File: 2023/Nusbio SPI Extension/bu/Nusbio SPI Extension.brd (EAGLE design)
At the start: 44 x 50 mm, 6 parts

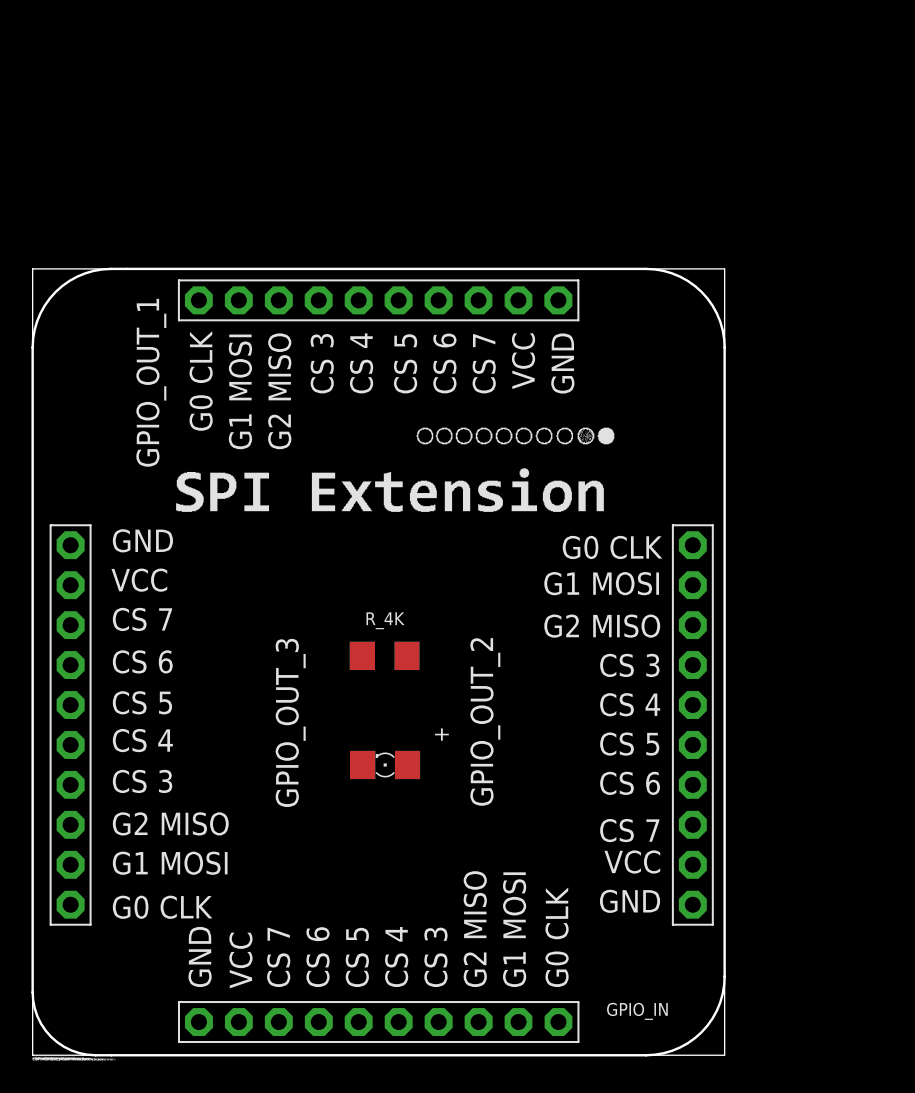
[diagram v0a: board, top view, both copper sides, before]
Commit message: Nusbio I2C Extension
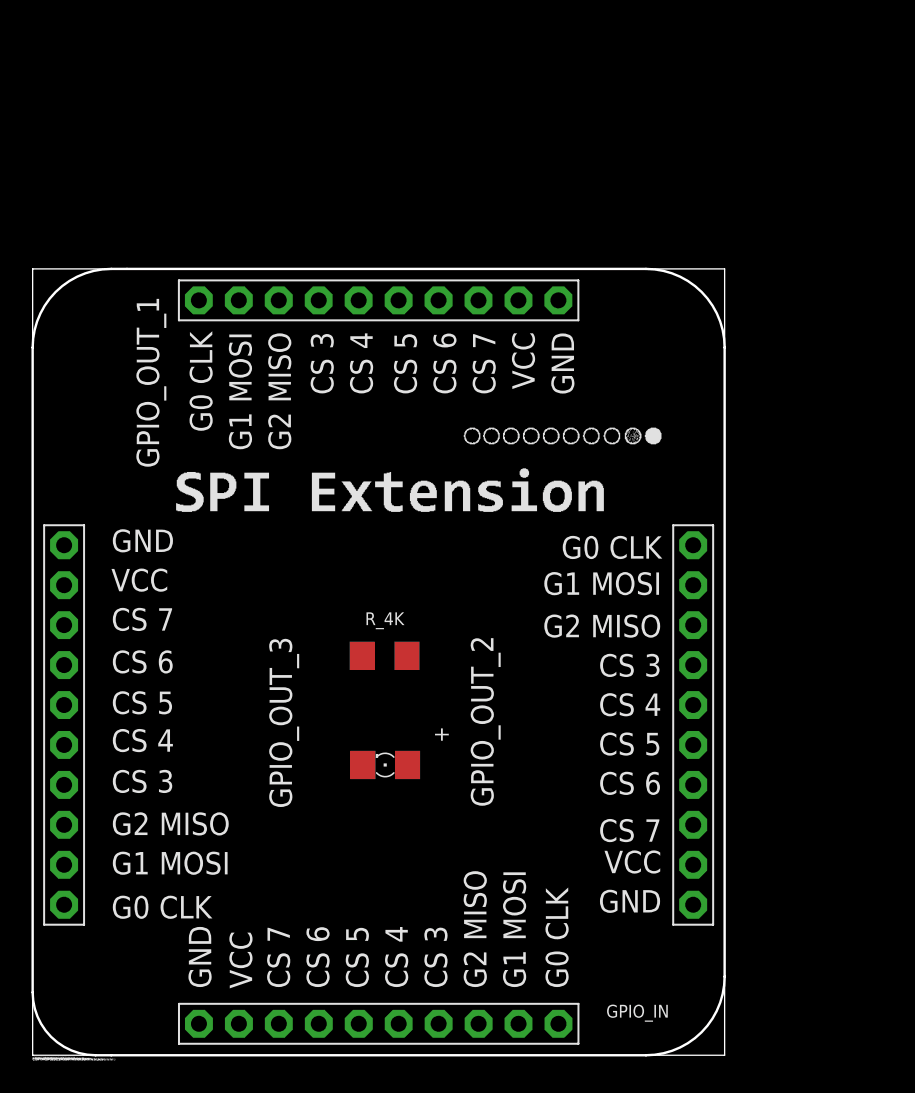
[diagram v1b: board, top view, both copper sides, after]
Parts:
- moved GPIO_OUT_3 0.41 mm to (2.00, 21.0)
- moved GPIO_IN 0.11 mm to (22.0, 2.00)

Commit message: Nusbio v2 pcb and SPIExtension v 1 2023/05
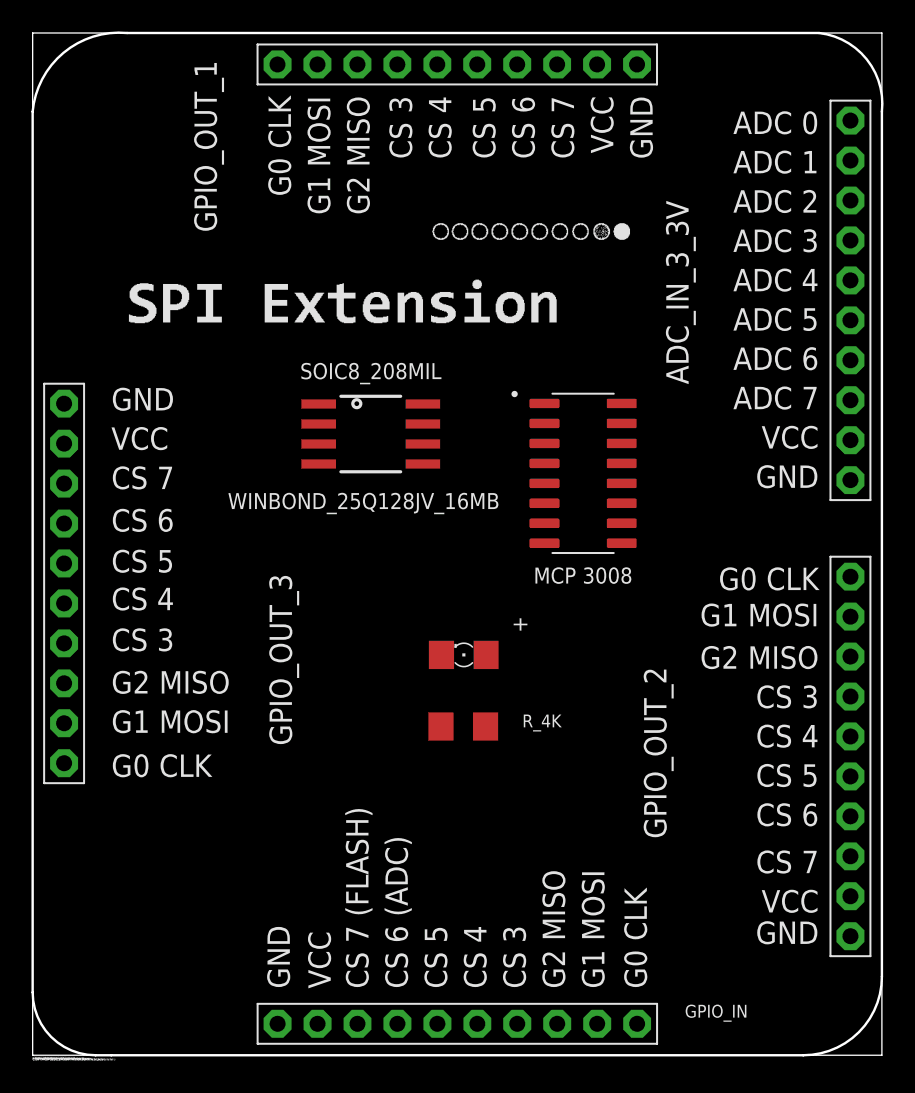
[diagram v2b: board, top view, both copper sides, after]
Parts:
- added ADC_IN_3_3V: PINHD-1X10, adafruit:1X10-BIG
- added MCP_3008_3_3V: MCP3008-I/SL, MCP3008-I_SL:SOIC127P600X175-16N
- added SOIC8_208MIL: (no value), microbuilder:SOIC8_208MIL
- moved GPIO_OUT_1 15.8 mm to (27.0, 63.0)
- moved GPIO_OUT_2 10.2 mm to (52.0, 19.0)
- moved GPIO_OUT_3 9.00 mm to (2.00, 30.0)
- moved LED_POWER 8.60 mm to (27.4, 25.5)
- moved R_4K 6.73 mm to (27.4, 20.9)
- moved GPIO_IN 5.00 mm to (27.0, 2.00)
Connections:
- new net ADC0: ADC_IN_3_3V.1, MCP_3008_3_3V.1
- new net ADC1: ADC_IN_3_3V.2, MCP_3008_3_3V.2
- new net ADC2: ADC_IN_3_3V.3, MCP_3008_3_3V.3
- new net ADC3: ADC_IN_3_3V.4, MCP_3008_3_3V.4
- new net ADC4: ADC_IN_3_3V.5, MCP_3008_3_3V.5
- new net ADC5: ADC_IN_3_3V.6, MCP_3008_3_3V.6
- new net ADC6: ADC_IN_3_3V.7, MCP_3008_3_3V.7
- new net ADC7: ADC_IN_3_3V.8, MCP_3008_3_3V.8
- net GND: now also ADC_IN_3_3V.10, MCP_3008_3_3V.14, MCP_3008_3_3V.9, SOIC8_208MIL.4
- net GPIO0: now also MCP_3008_3_3V.13, SOIC8_208MIL.6
- net GPIO1: now also MCP_3008_3_3V.11, SOIC8_208MIL.5
- net GPIO2: now also MCP_3008_3_3V.12, SOIC8_208MIL.2
- net GPIO6: now also MCP_3008_3_3V.10
- net GPIO7: now also SOIC8_208MIL.1
- net VCC: now also ADC_IN_3_3V.9, MCP_3008_3_3V.15, MCP_3008_3_3V.16, SOIC8_208MIL.3, SOIC8_208MIL.7, SOIC8_208MIL.8
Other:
- board size 44 x 50 mm -> 54 x 65 mm
- board text added: "ADC 0"
- board text added: "ADC 1"
- board text added: "ADC 2"
- board text added: "ADC 3"
- board text added: "ADC 4"
- board text added: "ADC 5"
- board text added: "ADC 6"
- board text added: "ADC 7"
- board text added: "CS 6 (ADC)"
- board text added: "CS 7 (FLASH)"
- board text added: "MCP 3008"
- board text added: "WINBOND_25Q128JV_16MB"

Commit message: Nusbio v2 pcb and SPIExtension v 1 2023/05
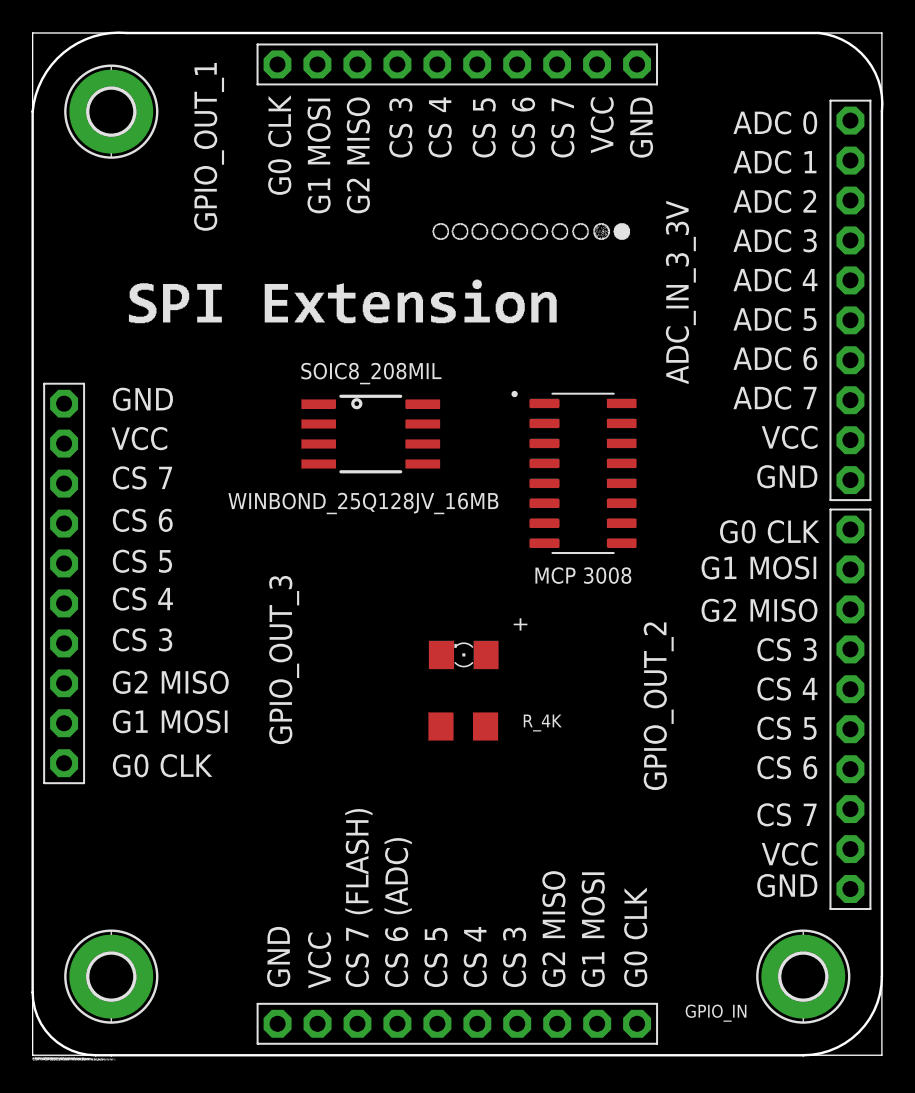
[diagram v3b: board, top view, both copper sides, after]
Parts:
- added H1, H2, H3: MOUNT-PAD-ROUND2.8, holes:2,8-PAD
- moved GPIO_OUT_2 3.00 mm to (52.0, 22.0)
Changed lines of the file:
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@@
 <text x="5" y="38.5" size="1.4224" layer="25" rot="R180" align="top-right">VCC</text>
 <text x="5" y="41" size="1.4224" layer="25" rot="R180" align="top-right">GND</text>
-<text x="50" y="28.7" size="1.4224" layer="25" rot="R180">G1 MOSI</text>
-<text x="50" y="26" size="1.4224" layer="25" rot="R180">G2 MISO</text>
-<text x="50" y="23.5" size="1.4224" layer="25" rot="R180">CS 3</text>
-<text x="50" y="21" size="1.4224" layer="25" rot="R180">CS 4</text>
-<text x="50" y="18.5" size="1.4224" layer="25" rot="R180">CS 5</text>
-<text x="50" y="16" size="1.4224" layer="25" rot="R180">CS 6</text>
-<text x="50" y="31" size="1.4224" layer="25" rot="R180">G0 CLK</text>
-<text x="50" y="13" size="1.4224" layer="25" rot="R180">CS 7</text>
-<text x="50" y="10.5" size="1.4224" layer="25" rot="R180">VCC</text>
-<text x="50" y="8.5" size="1.4224" layer="25" rot="R180">GND</text>
+<text x="50" y="31.7" size="1.4224" layer="25" rot="R180">G1 MOSI</text>
+<text x="50" y="29" size="1.4224" layer="25" rot="R180">G2 MISO</text>
+<text x="50" y="26.5" size="1.4224" layer="25" rot="R180">CS 3</text>
+<text x="50" y="24" size="1.4224" layer="25" rot="R180">CS 4</text>
+<text x="50" y="21.5" size="1.4224" layer="25" rot="R180">CS 5</text>
+<text x="50" y="19" size="1.4224" layer="25" rot="R180">CS 6</text>
+<text x="50" y="34" size="1.4224" layer="25" rot="R180">G0 CLK</text>
+<text x="50" y="16" size="1.4224" layer="25" rot="R180">CS 7</text>
+<text x="50" y="13.5" size="1.4224" layer="25" rot="R180">VCC</text>
+<text x="50" y="11.5" size="1.4224" layer="25" rot="R180">GND</text>
 <rectangle x1="6.488984375" y1="46.5478625" x2="7.136684375" y2="46.5940875" layer="25"/>
 <rectangle x1="19.7909625" y1="46.5478625" x2="20.3904" y2="46.5940875" layer="25"/>
@@
 <attribute name="VALUE" x="28.6878" y="27.9967" size="1.27" layer="27" rot="R180"/>
 </element>
-<element name="GPIO_OUT_2" library="adafruit" package="1X10-BIG" value="PINHD-1X10" x="52" y="19" smashed="yes" rot="R270">
-<attribute name="NAME" x="39.5898" y="19.231" size="1.4224" layer="25" ratio="10" rot="R270" align="center"/>
+<element name="GPIO_OUT_2" library="adafruit" package="1X10-BIG" value="PINHD-1X10" x="52" y="22" smashed="yes" rot="R270">
+<attribute name="NAME" x="39.5898" y="22.231" size="1.4224" layer="25" ratio="10" rot="R270" align="center"/>
 </element>
 <element name="GPIO_OUT_3" library="adafruit" package="1X10-BIG" value="PINHD-1X10" x="2" y="30" smashed="yes" rot="R90">
@@
 <attribute name="NAME" x="41" y="48.5" size="1.4224" layer="25" ratio="10" rot="R270" align="center"/>
 </element>
+<element name="H2" library="holes" library_urn="urn:adsk.eagle:library:237" package="2,8-PAD" package3d_urn="urn:adsk.eagle:package:14281/1" value="MOUNT-PAD-ROUND2.8" x="5" y="60" smashed="yes">
+<attribute name="POPULARITY" value="6" x="5" y="60" size="1.778" layer="27" display="off"/>
+</element>
+<element name="H1" library="holes" library_urn="urn:adsk.eagle:library:237" package="2,8-PAD" package3d_urn="urn:adsk.eagle:package:14281/1" value="MOUNT-PAD-ROUND2.8" x="5" y="5" smashed="yes">
+<attribute name="POPULARITY" value="6" x="5" y="5" size="1.778" layer="27" display="off"/>
+</element>
+<element name="H3" library="holes" library_urn="urn:adsk.eagle:library:237" package="2,8-PAD" package3d_urn="urn:adsk.eagle:package:14281/1" value="MOUNT-PAD-ROUND2.8" x="49" y="5" smashed="yes">
+<attribute name="POPULARITY" value="6" x="49" y="5" size="1.778" layer="27" display="off"/>
+</element>
 </elements>
 <signals>
@@
 <wire x1="18.185" y1="37.595" x2="37.455" y2="38.905" width="0" layer="19" extent="1-1"/>
 <wire x1="2" y1="41.43" x2="18.185" y2="37.595" width="0" layer="19" extent="1-1"/>
-<wire x1="52" y1="7.57" x2="28.7984" y2="20.8998" width="0" layer="19" extent="1-1"/>
+<wire x1="52" y1="10.57" x2="28.7984" y2="20.8998" width="0" layer="19" extent="1-1"/>
 </signal>
 <signal name="VCC">
@@
 <wire x1="28.8398" y1="25.4567" x2="24.815" y2="40.135" width="0" layer="19" extent="1-1"/>
 <wire x1="18.114771875" y1="2" x2="28.8398" y2="25.4567" width="0" layer="19" extent="1-1"/>
-<wire x1="52" y1="10.11" x2="28.8398" y2="25.4567" width="0" layer="19" extent="1-1"/>
+<wire x1="52" y1="13.11" x2="28.8398" y2="25.4567" width="0" layer="19" extent="1-1"/>
 </signal>
 <signal name="GPIO6">
@@
 <contactref element="MCP_3008_3_3V" pad="10"/>
 <wire x1="37.455" y1="33.825" x2="30.81" y2="63" width="0" layer="19" extent="1-1"/>
-<wire x1="52" y1="15.19" x2="37.455" y2="33.825" width="0" layer="19" extent="1-1"/>
-<wire x1="23.194771875" y1="2" x2="52" y2="15.19" width="0" layer="19" extent="1-1"/>
+<wire x1="52" y1="18.19" x2="37.455" y2="33.825" width="0" layer="19" extent="1-1"/>
+<wire x1="23.194771875" y1="2" x2="52" y2="18.19" width="0" layer="19" extent="1-1"/>
 <wire x1="2" y1="33.81" x2="23.194771875" y2="2" width="0" layer="19" extent="1-1"/>
 </signal>
@@
 <wire x1="2" y1="36.35" x2="18.185" y2="41.405" width="0" layer="19" extent="1-1"/>
 <wire x1="20.654771875" y1="2" x2="2" y2="36.35" width="0" layer="19" extent="1-1"/>
-<wire x1="52" y1="12.65" x2="20.654771875" y2="2" width="0" layer="19" extent="1-1"/>
+<wire x1="52" y1="15.65" x2="20.654771875" y2="2" width="0" layer="19" extent="1-1"/>
 </signal>
 <signal name="GPIO4">
@@
 <contactref element="GPIO_OUT_2" pad="5"/>
 <contactref element="GPIO_OUT_3" pad="5"/>
-<wire x1="52" y1="20.27" x2="25.73" y2="63" width="0" layer="19" extent="1-1"/>
-<wire x1="28.274771875" y1="2" x2="52" y2="20.27" width="0" layer="19" extent="1-1"/>
+<wire x1="52" y1="23.27" x2="25.73" y2="63" width="0" layer="19" extent="1-1"/>
+<wire x1="28.274771875" y1="2" x2="52" y2="23.27" width="0" layer="19" extent="1-1"/>
 <wire x1="2" y1="28.73" x2="28.274771875" y2="2" width="0" layer="19" extent="1-1"/>
 </signal>
@@
 <contactref element="GPIO_OUT_2" pad="4"/>
 <contactref element="GPIO_OUT_3" pad="4"/>
-<wire x1="52" y1="22.81" x2="23.19" y2="63" width="0" layer="19" extent="1-1"/>
-<wire x1="30.814771875" y1="2" x2="52" y2="22.81" width="0" layer="19" extent="1-1"/>
+<wire x1="52" y1="25.81" x2="23.19" y2="63" width="0" layer="19" extent="1-1"/>
+<wire x1="30.814771875" y1="2" x2="52" y2="25.81" width="0" layer="19" extent="1-1"/>
 <wire x1="2" y1="26.19" x2="30.814771875" y2="2" width="0" layer="19" extent="1-1"/>
 </signal>
@@
 <wire x1="18.185" y1="40.135" x2="20.65" y2="63" width="0" layer="19" extent="1-1"/>
 <wire x1="37.455" y1="36.365" x2="18.185" y2="40.135" width="0" layer="19" extent="1-1"/>
-<wire x1="52" y1="25.35" x2="37.455" y2="36.365" width="0" layer="19" extent="1-1"/>
+<wire x1="52" y1="28.35" x2="37.455" y2="36.365" width="0" layer="19" extent="1-1"/>
 <wire x1="2" y1="23.65" x2="18.185" y2="40.135" width="0" layer="19" extent="1-1"/>
-<wire x1="33.354771875" y1="2" x2="52" y2="25.35" width="0" layer="19" extent="1-1"/>
+<wire x1="33.354771875" y1="2" x2="52" y2="28.35" width="0" layer="19" extent="1-1"/>
 </signal>
 <signal name="GPIO1">
@@
 <wire x1="24.815" y1="37.595" x2="18.11" y2="63" width="0" layer="19" extent="1-1"/>
 <wire x1="37.455" y1="35.095" x2="24.815" y2="37.595" width="0" layer="19" extent="1-1"/>
-<wire x1="52" y1="27.89" x2="37.455" y2="35.095" width="0" layer="19" extent="1-1"/>
+<wire x1="52" y1="30.89" x2="37.455" y2="35.095" width="0" layer="19" extent="1-1"/>
 <wire x1="2" y1="21.11" x2="24.815" y2="37.595" width="0" layer="19" extent="1-1"/>
-<wire x1="35.894771875" y1="2" x2="52" y2="27.89" width="0" layer="19" extent="1-1"/>
+<wire x1="35.894771875" y1="2" x2="52" y2="30.89" width="0" layer="19" extent="1-1"/>
 </signal>
 <signal name="GPIO0">
@@
 <contactref element="SOIC8_208MIL" pad="6"/>
 <contactref element="MCP_3008_3_3V" pad="13"/>
-<wire x1="37.455" y1="37.635" x2="52" y2="30.43" width="0" layer="19" extent="1-1"/>
+<wire x1="37.455" y1="37.635" x2="52" y2="33.43" width="0" layer="19" extent="1-1"/>
 <wire x1="24.815" y1="38.865" x2="37.455" y2="37.635" width="0" layer="19" extent="1-1"/>
 <wire x1="15.57" y1="63" x2="24.815" y2="38.865" width="0" layer="19" extent="1-1"/>
-<wire x1="38.434771875" y1="2" x2="52" y2="30.43" width="0" layer="19" extent="1-1"/>
+<wire x1="38.434771875" y1="2" x2="52" y2="33.43" width="0" layer="19" extent="1-1"/>
 <wire x1="2" y1="18.57" x2="24.815" y2="38.865" width="0" layer="19" extent="1-1"/>
 </signal>
@@
 <contactref element="GPIO_OUT_2" pad="6"/>
 <contactref element="GPIO_OUT_3" pad="6"/>
-<wire x1="52" y1="17.73" x2="28.27" y2="63" width="0" layer="19" extent="1-1"/>
-<wire x1="25.734771875" y1="2" x2="52" y2="17.73" width="0" layer="19" extent="1-1"/>
+<wire x1="52" y1="20.73" x2="28.27" y2="63" width="0" layer="19" extent="1-1"/>
+<wire x1="25.734771875" y1="2" x2="52" y2="20.73" width="0" layer="19" extent="1-1"/>
 <wire x1="2" y1="31.27" x2="25.734771875" y2="2" width="0" layer="19" extent="1-1"/>
 </signal>
@@
 </board>
 </drawing>
+<compatibility>
+<note version="8.2" severity="warning">
+Since Version 8.2, EAGLE supports online libraries. The ids
+of those online libraries will not be understood (or retained)
+with this version.
+</note>
+<note version="8.3" severity="warning">
+Since Version 8.3, EAGLE supports URNs for individual library
+assets (packages, symbols, and devices). The URNs of those assets
+will not be understood (or retained) with this version.
+</note>
+<note version="8.3" severity="warning">
+Since Version 8.3, EAGLE supports the association of 3D packages
+with devices in libraries, schematics, and board files. Those 3D
+packages will not be understood (or retained) with this version.
+</note>
+</compatibility>
 </eagle>
